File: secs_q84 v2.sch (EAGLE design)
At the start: 105 parts, among them IC1 MAX203ECWP, IC2 REF3440TIDBVR, IC3 ADP151AUJZ-3.3-R7, IC4 PIC18F47Q84-I_PT, IC5 MCZ33996EK, IC6 74HC125D, IC7 TIC12400DCPR

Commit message: add frame
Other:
- note removed: "5/6 and 8/9 pins swapped as a fix"
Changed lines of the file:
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@@
 <part name="VDD27" library="supply1" library_urn="urn:adsk.eagle:library:371" deviceset="VDD" device=""/>
 <part name="P+3" library="supply1" library_urn="urn:adsk.eagle:library:371" deviceset="VCC" device=""/>
+<part name="FRAME1" library="frames" library_urn="urn:adsk.eagle:library:229" deviceset="FRAME_C_L" device=""/>
 </parts>
 <sheets>
 <sheet>
 <plain>
-<text x="332.74" y="-20.32" size="1.778" layer="91">5/6 and 8/9 pins swapped as a fix</text>
 </plain>
 <instances>
@@
 <attribute name="VALUE" x="58.42" y="71.12" size="1.778" layer="96" rot="R180"/>
 </instance>
+<instance part="FRAME1" gate="G$1" x="-142.24" y="-223.52" smashed="yes"/>
+<instance part="FRAME1" gate="G$2" x="309.88" y="-223.52" smashed="yes">
+<attribute name="LAST_DATE_TIME" x="322.58" y="-222.25" size="2.54" layer="94"/>
+<attribute name="SHEET" x="396.24" y="-222.25" size="2.54" layer="94"/>
+<attribute name="DRAWING_NAME" x="327.66" y="-204.47" size="2.54" layer="94"/>
+</instance>
 </instances>

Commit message: PCB updates:wq
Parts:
- added C29: 10uf, rcl:C-USC0805
- added INT_RESET: reset, jumper:SJ
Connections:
- net MCZ_PWM: now also INT_RESET.2
- net R_RESET: now also C29.1, INT_RESET.1
- net VSS: now also C29.2
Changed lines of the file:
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@@
 <part name="P+3" library="supply1" library_urn="urn:adsk.eagle:library:371" deviceset="VCC" device=""/>
 <part name="FRAME1" library="frames" library_urn="urn:adsk.eagle:library:229" deviceset="FRAME_C_L" device=""/>
+<part name="C29" library="rcl" library_urn="urn:adsk.eagle:library:334" deviceset="C-US" device="C0805" package3d_urn="urn:adsk.eagle:package:23617/2" value="10uf"/>
+<part name="VSS73" library="supply1" library_urn="urn:adsk.eagle:library:371" deviceset="VSS" device=""/>
+<part name="INT_RESET" library="jumper" library_urn="urn:adsk.eagle:library:252" deviceset="SJ" device="" package3d_urn="urn:adsk.eagle:package:15471/1" value="reset"/>
 </parts>
 <sheets>
@@
 <instance part="R5" gate="G$1" x="20.32" y="66.04" smashed="yes">
 <attribute name="NAME" x="16.51" y="67.5386" size="1.778" layer="95"/>
-<attribute name="VALUE" x="16.51" y="62.738" size="1.778" layer="96"/>
+<attribute name="VALUE" x="21.59" y="67.818" size="1.778" layer="96"/>
 </instance>
 <instance part="R6" gate="G$1" x="10.16" y="86.36" smashed="yes" rot="R90">
@@
 </instance>
 <instance part="VSS6" gate="G$1" x="10.16" y="71.12" smashed="yes">
-<attribute name="VALUE" x="12.7" y="66.04" size="1.778" layer="96" rot="R180"/>
+<attribute name="VALUE" x="7.62" y="73.66" size="1.778" layer="96" rot="R180"/>
 </instance>
 <instance part="C2" gate="G$1" x="93.98" y="-5.08" smashed="yes">
@@
 <instance part="FRAME1" gate="G$2" x="309.88" y="-223.52" smashed="yes">
 <attribute name="LAST_DATE_TIME" x="322.58" y="-222.25" size="2.54" layer="94"/>
-<attribute name="SHEET" x="396.24" y="-222.25" size="2.54" layer="94"/>
+<attribute name="SHEET" x="383.54" y="-196.85" size="2.54" layer="94" display="both"/>
 <attribute name="DRAWING_NAME" x="327.66" y="-204.47" size="2.54" layer="94"/>
 </instance>
+<instance part="C29" gate="G$1" x="15.24" y="58.42" smashed="yes">
+<attribute name="NAME" x="16.256" y="53.975" size="1.778" layer="95"/>
+<attribute name="VALUE" x="6.096" y="51.689" size="1.778" layer="96"/>
+</instance>
+<instance part="VSS73" gate="G$1" x="15.24" y="50.8" smashed="yes">
+<attribute name="VALUE" x="17.78" y="45.72" size="1.778" layer="96" rot="R180"/>
+</instance>
+<instance part="INT_RESET" gate="1" x="10.16" y="63.5" smashed="yes" rot="R180">
+<attribute name="NAME" x="12.7" y="60.96" size="1.778" layer="95" rot="R180"/>
+<attribute name="VALUE" x="12.7" y="67.31" size="1.778" layer="96" rot="R180"/>
+</instance>
 </instances>
 <busses>
@@
 <junction x="170.18" y="-172.72"/>
 </segment>
+<segment>
+<pinref part="C29" gate="G$1" pin="2"/>
+<pinref part="VSS73" gate="G$1" pin="VSS"/>
+<junction x="15.24" y="53.34"/>
+</segment>
 </net>
 <net name="CPU_CLK" class="0">
@@
 <segment>
 <pinref part="R5" gate="G$1" pin="1"/>
-<wire x1="15.24" y1="66.04" x2="15.24" y2="81.28" width="0.1524" layer="91"/>
+<wire x1="15.24" y1="60.96" x2="15.24" y2="63.5" width="0.1524" layer="91"/>
 <pinref part="R6" gate="G$1" pin="1"/>
 <pinref part="C1" gate="G$1" pin="1"/>
+<wire x1="15.24" y1="63.5" x2="15.24" y2="66.04" width="0.1524" layer="91"/>
+<wire x1="15.24" y1="66.04" x2="15.24" y2="81.28" width="0.1524" layer="91"/>
 <wire x1="15.24" y1="81.28" x2="10.16" y2="81.28" width="0.1524" layer="91"/>
 <junction x="10.16" y="81.28"/>
-<junction x="15.24" y="66.04"/>
+<junction x="15.24" y="60.96"/>
 <pinref part="RESET" gate="1" pin="1"/>
 <label x="15.24" y="71.12" size="1.778" layer="95"/>
+<pinref part="C29" gate="G$1" pin="1"/>
+<wire x1="15.24" y1="60.96" x2="15.24" y2="63.5" width="0.1524" layer="91"/>
+<junction x="15.24" y="66.04"/>
+<pinref part="INT_RESET" gate="1" pin="1"/>
+<wire x1="15.24" y1="63.5" x2="15.24" y2="66.04" width="0.1524" layer="91"/>
+<junction x="15.24" y="63.5"/>
 </segment>
 <segment>
@@
 <label x="124.46" y="-58.42" size="1.778" layer="95"/>
 </segment>
+<segment>
+<wire x1="-7.62" y1="63.5" x2="5.08" y2="63.5" width="0.1524" layer="91"/>
+<pinref part="INT_RESET" gate="1" pin="2"/>
+<junction x="5.08" y="63.5"/>
+<junction x="-7.62" y="63.5"/>
+<label x="-22.86" y="63.5" size="1.778" layer="95"/>
+</segment>
 </net>
 <net name="SDI2" class="0">
@@
 </sheet>
 </sheets>
+<errors>
+</errors>
 </schematic>
 </drawing>

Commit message: up
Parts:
- removed INT_RESET: reset, jumper:SJ
- added INT_RESET1: int_reset, pinhead:PINHD-1X2
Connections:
- net MCZ_PWM: now also INT_RESET1.2; no longer INT_RESET.2
- net R_RESET: now also INT_RESET1.1; no longer INT_RESET.1
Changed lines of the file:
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@@
 <part name="C29" library="rcl" library_urn="urn:adsk.eagle:library:334" deviceset="C-US" device="C0805" package3d_urn="urn:adsk.eagle:package:23617/2" value="10uf"/>
 <part name="VSS73" library="supply1" library_urn="urn:adsk.eagle:library:371" deviceset="VSS" device=""/>
-<part name="INT_RESET" library="jumper" library_urn="urn:adsk.eagle:library:252" deviceset="SJ" device="" package3d_urn="urn:adsk.eagle:package:15471/1" value="reset"/>
+<part name="INT_RESET1" library="pinhead" library_urn="urn:adsk.eagle:library:325" deviceset="PINHD-1X2" device="" package3d_urn="urn:adsk.eagle:package:22435/2" value="int_reset"/>
 </parts>
 <sheets>
@@
 <attribute name="VALUE" x="17.78" y="45.72" size="1.778" layer="96" rot="R180"/>
 </instance>
-<instance part="INT_RESET" gate="1" x="10.16" y="63.5" smashed="yes" rot="R180">
-<attribute name="NAME" x="12.7" y="60.96" size="1.778" layer="95" rot="R180"/>
-<attribute name="VALUE" x="12.7" y="67.31" size="1.778" layer="96" rot="R180"/>
+<instance part="INT_RESET1" gate="G$1" x="2.54" y="63.5" smashed="yes" rot="R180">
+<attribute name="NAME" x="8.89" y="57.785" size="1.778" layer="95" rot="R180"/>
+<attribute name="VALUE" x="-1.27" y="63.5" size="1.778" layer="96" rot="R180"/>
 </instance>
 </instances>
@@
 <segment>
 <pinref part="R5" gate="G$1" pin="1"/>
-<wire x1="15.24" y1="60.96" x2="15.24" y2="63.5" width="0.1524" layer="91"/>
 <pinref part="R6" gate="G$1" pin="1"/>
 <pinref part="C1" gate="G$1" pin="1"/>
-<wire x1="15.24" y1="63.5" x2="15.24" y2="66.04" width="0.1524" layer="91"/>
 <wire x1="15.24" y1="66.04" x2="15.24" y2="81.28" width="0.1524" layer="91"/>
 <wire x1="15.24" y1="81.28" x2="10.16" y2="81.28" width="0.1524" layer="91"/>
@@
 <wire x1="15.24" y1="60.96" x2="15.24" y2="63.5" width="0.1524" layer="91"/>
 <junction x="15.24" y="66.04"/>
-<pinref part="INT_RESET" gate="1" pin="1"/>
 <wire x1="15.24" y1="63.5" x2="15.24" y2="66.04" width="0.1524" layer="91"/>
 <junction x="15.24" y="63.5"/>
+<pinref part="INT_RESET1" gate="G$1" pin="1"/>
+<wire x1="5.08" y1="60.96" x2="15.24" y2="60.96" width="0.1524" layer="91"/>
+<junction x="5.08" y="60.96"/>
 </segment>
 <segment>
@@
 <segment>
 <wire x1="-7.62" y1="63.5" x2="5.08" y2="63.5" width="0.1524" layer="91"/>
-<pinref part="INT_RESET" gate="1" pin="2"/>
-<junction x="5.08" y="63.5"/>
 <junction x="-7.62" y="63.5"/>
 <label x="-22.86" y="63.5" size="1.778" layer="95"/>
-</segment>
-</net>
+<pinref part="INT_RESET1" gate="G$1" pin="2"/>
+<junction x="5.08" y="63.5"/>
+</segment>
+</net>

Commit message: up uuuppp#	modified:   secs_q84 v2.b#5
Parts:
- removed IC4: PIC18F47Q84-I_PT, PIC18F47Q84-I_PT:PIC18F47Q84-I_PT
- removed R27: 4.7k, rcl:R-US_R0805
- added IC8: PIC18F57Q84-I_PT, PIC18F57Q84-I_PT:PIC18F57Q84-I_PT
- added R31: 4.7k, rcl:R-US_R0805
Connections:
- net +3V3: now also R31.2; no longer R27.2
- net ANA0: now also IC8.RA0; no longer IC4.RA0
- net ANA1: now also IC8.RA1; no longer IC4.RA1
- net ANA2: now also IC8.RA2; no longer IC4.RA2
- net ANA4: now also IC8.RA4; no longer IC4.RA4
- net ANA5: now also IC8.RA5; no longer IC4.RA5
- net ANC6: now also IC8.RC6; no longer IC4.RC6
- net ANC7: now also IC8.RC7; no longer IC4.RC7
- net AND5: now also IC8.RD5; no longer IC4.RD5
- net CLOCKO: now also IC8.RA6; no longer IC4.RA6
- net CPU_CLK: now also IC8.RA7; no longer IC4.RA7
- net CS: now also IC8.RD3; no longer IC4.RD3
- net DLED: now also IC8.RB3, IC8.RD4; no longer IC4.RB3, IC4.RD4
- net MB_RX: now also IC8.RC0; no longer IC4.RC0
- net MB_TX: now also IC8.RC1; no longer IC4.RC1
- net MCLR_SIG: now also IC8.VPP/!MCLR!/RE3; no longer IC4.VPP/!MCLR!/RE3
- net MCZ_CS: now also IC8.RE0; no longer IC4.RE0
- net MCZ_PWM: now also IC8.RD7; no longer IC4.RD7
- net MLED: now also IC8.RB1; no longer IC4.RB1
- net PC_RX2: now also IC8.RD0; no longer IC4.RD0
- net PC_TX2: now also IC8.RD6; no longer IC4.RD6
- net PGC_TICINT: now also IC8.ICSPCLK/RB6; no longer IC4.ICSPCLK/RB6
- net PGD_DAC1: now also IC8.ICSPDAT/RB7; no longer IC4.ICSPDAT/RB7
- net RLED: now also IC8.RB2; no longer IC4.RB2
- net SCK1: now also IC8.RC3; no longer IC4.RC3
- net SCK2: now also IC8.RD2; no longer IC4.RD2
- net SDI1: now also IC8.RC4; no longer IC4.RC4
- net SDI2: now also IC8.RB5; no longer IC4.RB5
- net SDO1: now also IC8.RC5; no longer IC4.RC5
- net SDO2: now also IC8.RB4; no longer IC4.RB4
- net SPI2_REQ: now also IC8.RB0, R31.1; no longer IC4.RB0, R27.1
- net SS2: now also IC8.RD1; no longer IC4.RD1
- net SS_CS: now also IC8.RE2; no longer IC4.RE2
- net TIC_CS: now also IC8.RE1; no longer IC4.RE1
- net TP1_TEST_SIG: now also IC8.RC2; no longer IC4.RC2
- net VDD: now also IC8.VDD_1, IC8.VDD_2; no longer IC4.VDD_1, IC4.VDD_2
- net VREF_4.1: now also IC8.RA3; no longer IC4.RA3
- net VSS: now also IC8.EP, IC8.VSS_1, IC8.VSS_2; no longer IC4.VSS_1, IC4.VSS_2

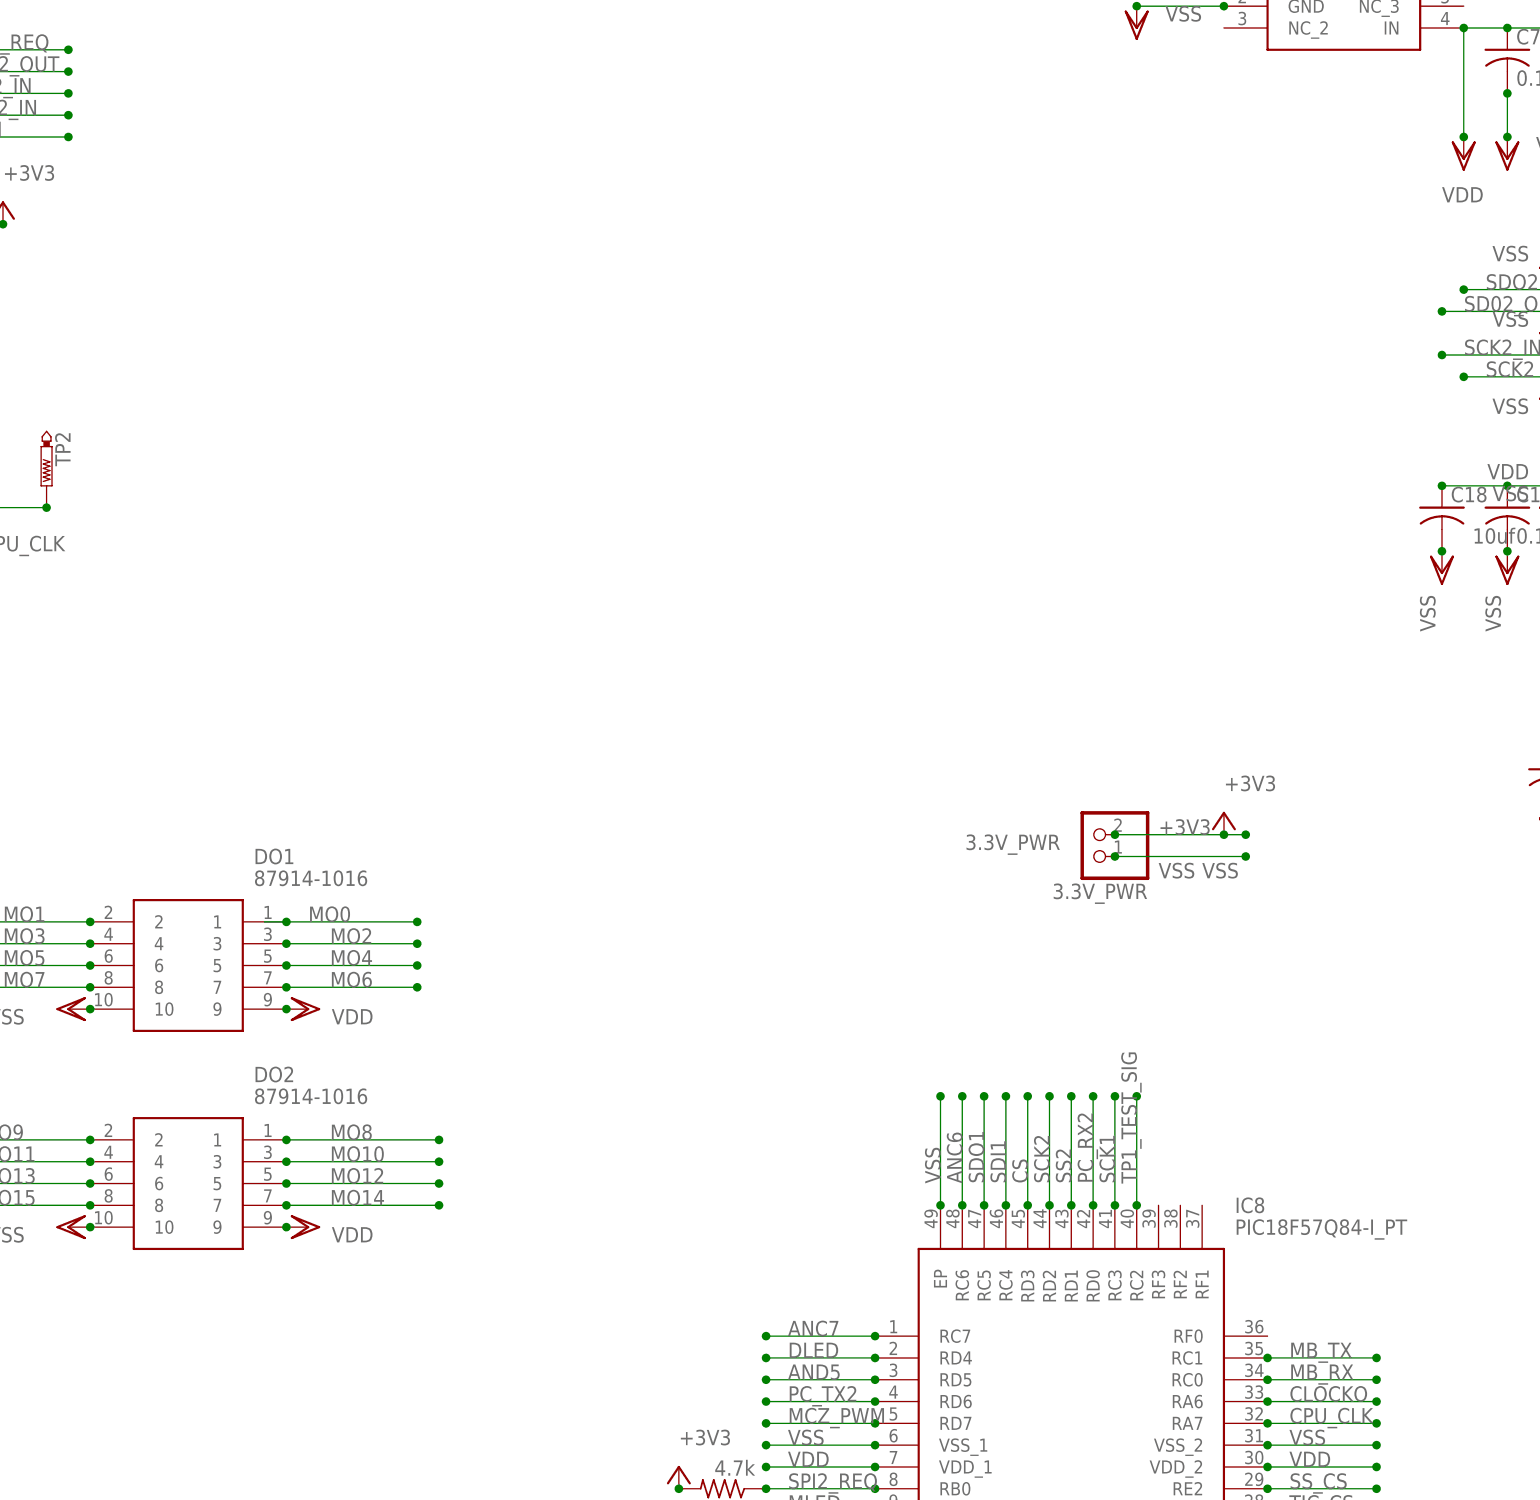
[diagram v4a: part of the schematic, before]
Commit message: 57Q84 support
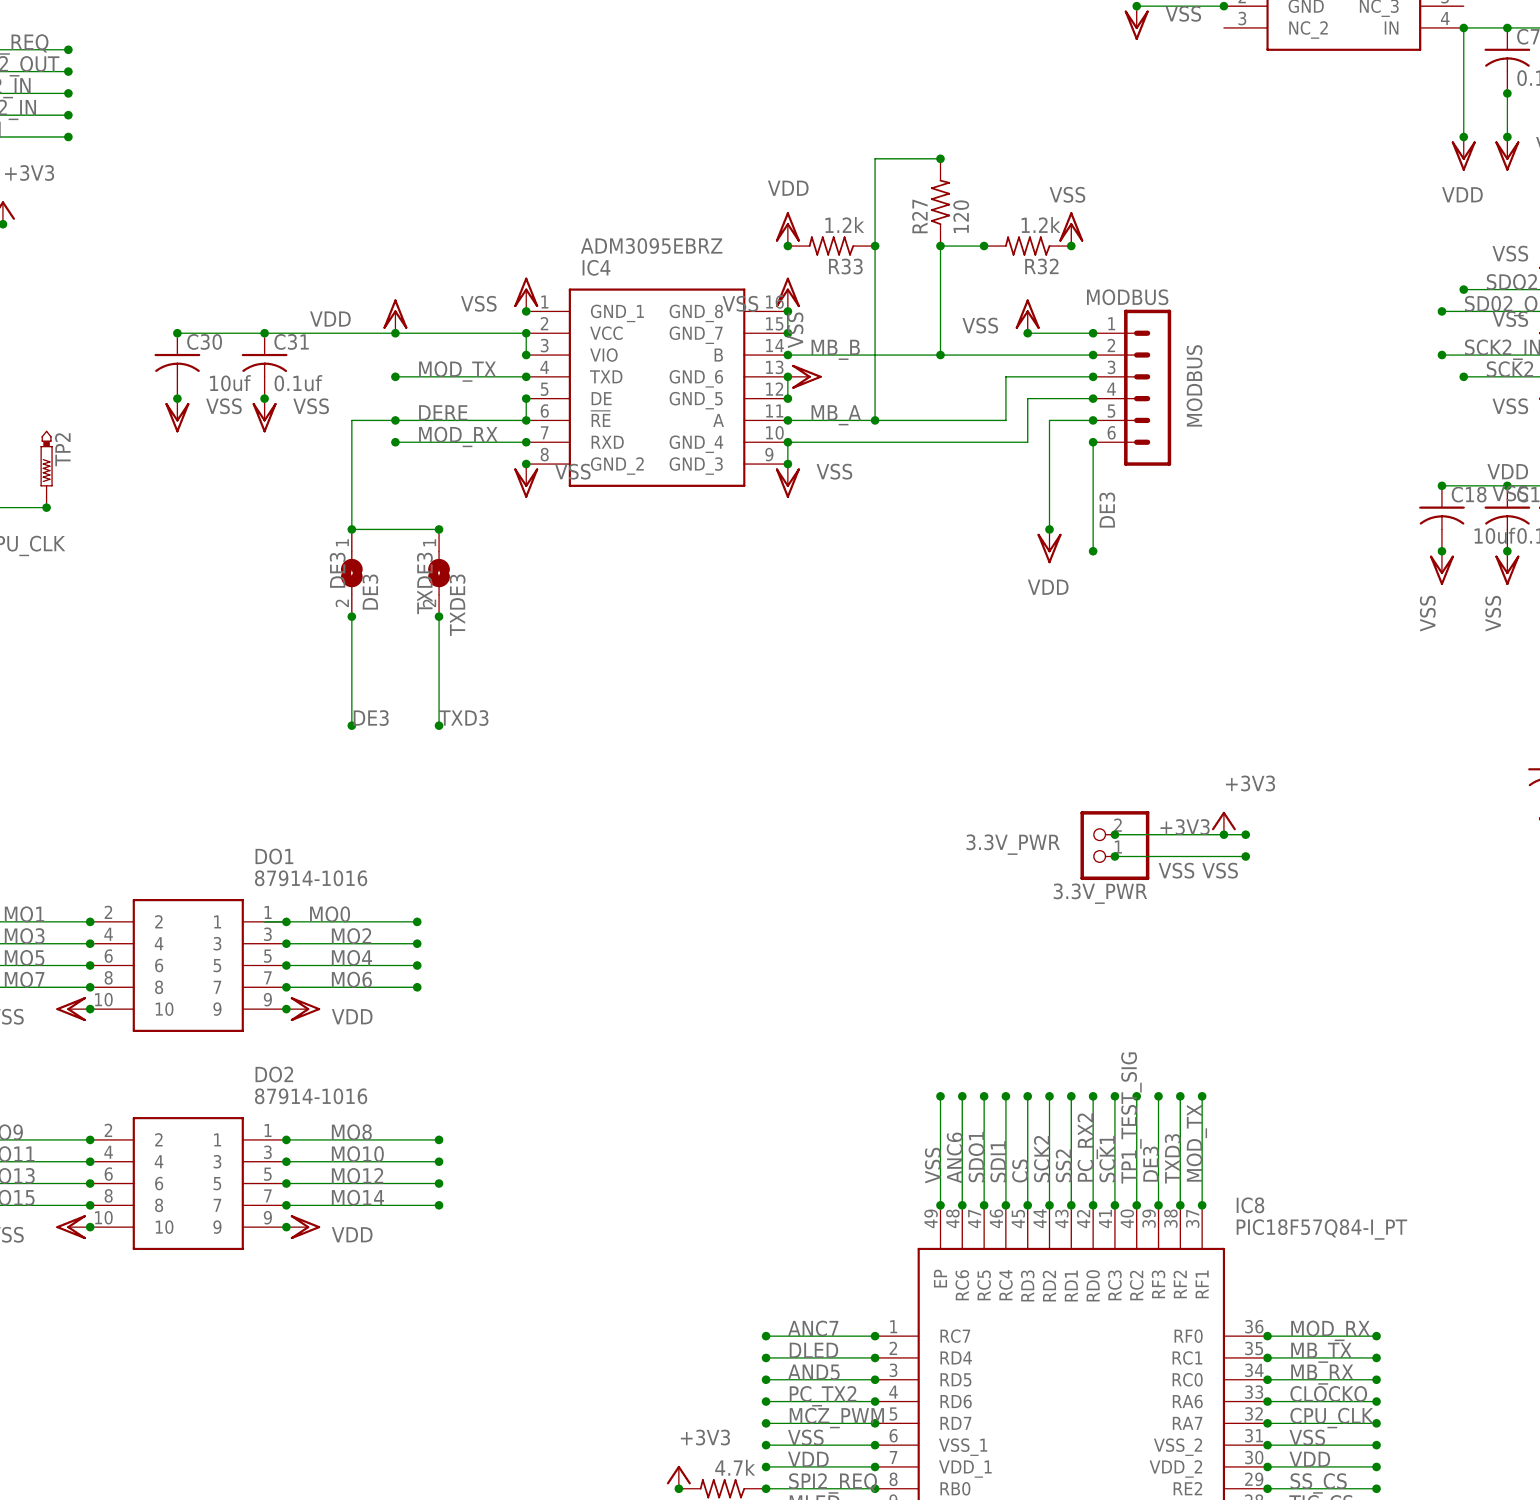
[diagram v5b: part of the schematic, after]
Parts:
- added C30: 10uf, rcl:C-USC0805
- added C31: 0.1uf, rcl:C-USC0805
- added DE3: DE3, jumper:SJ
- added IC4: ADM3095EBRZ, ADM3095EBRZ:ADM3095EBRZ
- added MODBUS: MODBUS, con-lstb:MA06-1
- added R27: 120, rcl:R-US_R0805
- added R32, R33: 1.2k, rcl:R-US_R0805
- added TXDE3: TXDE3, jumper:SJ
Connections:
- new net DE3: DE3.2, IC8.RF3, MODBUS.6
- new net DERE: DE3.1, IC4.!RE, IC4.DE, TXDE3.1
- new net MB_A: IC4.A, MODBUS.3, R27.2, R33.1
- new net MB_B: IC4.B, MODBUS.2, R27.1, R32.2
- new net MOD_RX: IC4.RXD, IC8.RF0
- new net MOD_TX: IC4.TXD, IC8.RF1
- new net TXD3: IC8.RF2, TXDE3.2
- net VDD: now also C30.1, C31.1, IC4.VCC, IC4.VIO, MODBUS.5, R33.2
- net VSS: now also C30.2, C31.2, IC4.GND_1, IC4.GND_2, IC4.GND_3, IC4.GND_4, IC4.GND_5, IC4.GND_6, IC4.GND_7, IC4.GND_8, MODBUS.1, MODBUS.4, R32.1
